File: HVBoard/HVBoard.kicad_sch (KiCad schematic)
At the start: 40 parts, among them J1 Conn_01x03_Pin, J2 Conn_01x08_Pin, K1 G2RL-1A-E-HA DC5, K2 G2RL-1A-E-HA DC5, Q1 NMOS, Q2 NMOS, Q3 BTA16-600B, Q4 NMOS, Q5 BTA16-600B, Q6 NMOS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

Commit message: More work
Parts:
- removed C1, C2: 0.01u, symbol Device:C_Polarized
- removed J1: Conn_01x03_Pin, symbol Connector:Conn_01x03_Pin
- removed PS1: TMLM04105, Converter_ACDC:Converter_ACDC_TRACO_TMLM-04_THT, symbol Converter_ACDC:TMLM04105
- added C1, C3: 0.01u, Capacitor_THT:C_Rect_L13.0mm_W4.0mm_P10.00mm_FKS3_FKP3_MKS4, symbol Device:C
- added H5, H6: MountingHole, MountingHole:MountingHole_3.2mm_M3, symbol Mechanical:MountingHole
- added J1: Conn_01x08_Pin, Connector_PinHeader_2.54mm:PinHeader_1x08_P2.54mm_Vertical, symbol Connector:Conn_01x08_Pin
- added J3: B3P-VH__LF__SN_, HWBoard:HDRV3W114P0X396_1X3_1182X850X1090P, symbol B3P-VH:B3P-VH__LF__SN_
- added J4, J5: Conn_01x02_Pin, symbol Connector:Conn_01x02_Pin
- added J6: Conn_01x03_Pin, symbol Connector:Conn_01x03_Pin
- added R16: R, Resistor_SMD:R_0603_1608Metric_Pad0.98x0.95mm_HandSolder, symbol Device:R
- added U4: 5V700mA 3.5W, wx-dc12003:WX-DC12003, symbol WX-DC12003:WX-DC12003
- Q1, Q2, Q4, Q6: footprint (none) -> Package_TO_SOT_SMD:SOT-23
- R11, R14, R3, R5, R6, R9: footprint (none) -> Resistor_SMD:R_1206_3216Metric_Pad1.30x1.75mm_HandSolder
- R13, R8: footprint (none) -> Resistor_THT:R_Axial_DIN0207_L6.3mm_D2.5mm_P10.16mm_Horizontal
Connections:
- net +3.3V: now also R16.2
- net +5V: now also J6.3 (Pin_3)
- net 120VAC_HOT: now also K1.13, U4.2 (L); no longer K1.14
- net 120VAC_HOT_SWITCHED: now also K1.14; no longer K1.13
- net 120VAC_NEUTRAL: now also K2.13, U4.1 (N); no longer K2.14
- net 120VAC_NEUTRAL_SWITCHED: now also K2.14, J3.3; no longer K2.13
- net ACDC_5V: now also U4.3 (V+)
- net BOILER_HOT_OUT: now also C1.2
- net GND: now also J1.8 (Pin_8), J5.1 (Pin_1), J6.1 (Pin_1), U4.4 (V-)
- net PUMP_HOT_OUT: now also C3.2, J3.1
- net at R13.2: now also C1.1
- net at R8.2: now also C3.1
- new net PRESSURE_SENSOR_SIG: J6.2 (Pin_2)
- new net STEAM_VALVE_IN: J5.2 (Pin_2), R16.1
- new net THERMISTOR_IN: J4.2 (Pin_2)
- new net THERMISTOR_OUT: J4.1 (Pin_1)
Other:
- note added: "Capacitors: MKT1822310405"
- note added: "Mounting holes"
- note added: "NTC Thermistor"
- note added: "Pump connector is B3P-VH"
- note added: "Resistors: 1W Metal Film"
- note added: "Steam Valve Switch"
- note removed: "Pump connector is B3P-VH?"

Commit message: More HV work
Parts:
- removed D2: D_Zener, symbol Device:D_Zener
- removed H1, H2, H3, H4: MountingHole_Pad_MP, symbol Mechanical:MountingHole_Pad_MP
- removed K2: G2RL-1A-E-HA DC5, Relay_THT:Relay_SPST_Omron_G2RL-1A-E, symbol Relay:G2RL-1A-E
- removed Q2: NMOS, Package_TO_SOT_SMD:SOT-23, symbol Simulation_SPICE:NMOS
- added D2: PTVS6V0S1UR-QX, Diode_SMD:Nexperia_CFP3_SOD-123W, symbol Diode:ESD5Zxx
- added D3: MP01EA06, Diode_SMD:D_SOD-123, symbol Device:D_Schottky
- added D4: LED, LED_SMD:LED_0603_1608Metric, symbol Device:LED
- added F1: 1A, symbol Device:Fuse
- added J7, J8: Screw_Terminal_01x02, TerminalBlock:TerminalBlock_bornier-2_P5.08mm, symbol Connector:Screw_Terminal_01x02
- added JP1: Jumper_2_Open, symbol Jumper:Jumper_2_Open
- added R17: 20k, Resistor_SMD:R_0603_1608Metric_Pad0.98x0.95mm_HandSolder, symbol Device:R
- added TP6: TestPoint, Connector_PinHeader_2.54mm:PinHeader_1x01_P2.54mm_Vertical, symbol Connector:TestPoint
- D1: footprint (none) -> Diode_SMD:D_SOD-123
- J1, J2: footprint Connector_PinHeader_2.54mm:PinHeader_1x08_P2.54mm_Vertical -> Connector_JST:JST_PH_B8B-PH-K_1x08_P2.00mm_Vertical
- J4, J5: footprint (none) -> Connector_JST:JST_XH_B2B-XH-AM_1x02_P2.50mm_Vertical
- J6: footprint (none) -> Connector_JST:JST_XH_B3B-XH-AM_1x03_P2.50mm_Vertical
- R12, R7: value 65 -> 220
- R2: value 10k -> 220; footprint Resistor_SMD:R_0603_1608Metric_Pad0.98x0.95mm_HandSolder -> Resistor_SMD:R_0603_1608Metric; Mouser # (none) -> 71-CRCW0603-665-E3; Mouser Link (none) -> https://www.mouser.com/ProductDetail/Vishay-Dale/CRCW060366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
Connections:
- net 120VAC_NEUTRAL_SWITCHED is gone; now on net 120VAC_NEUTRAL: J3.3, R5.2
- net +3.3V: no longer J2.2 (Pin_2), R12.1, R4.1, R7.1
- net +5V: now also R12.1, R2.1, R4.2, R7.1, D3.1 (K)
- net 120VAC_HOT: now also J7.2 (Pin_2)
- net 120VAC_NEUTRAL: now also J7.1 (Pin_1), J8.2 (Pin_2)
- net ACDC_5V: now also JP1.1 (A); no longer J2.3 (Pin_3)
- net AC_RELAYS: now also J2.2 (Pin_2); no longer J2.4 (Pin_4), R2.1
- net AC_ZC: now also J2.3 (Pin_3), R4.1, R17.1; no longer J2.5 (Pin_5), R4.2
- net BOILER_HOT_OUT: now also J8.1 (Pin_1)
- net BOILER_TRIAC: now also J2.5 (Pin_5); no longer J2.7 (Pin_7)
- net GND: now also D2.2 (A), D4.1 (K), R17.2
- net PRESSURE_SENSOR_SIG: now also J2.7 (Pin_7)
- net PUMP_TRIAC: now also J2.4 (Pin_4); no longer J2.6 (Pin_6)
- net STEAM_VALVE_IN: now also J2.6 (Pin_6)
- net THERMISTOR_IN: now also J1.1 (Pin_1)
- net THERMISTOR_OUT: now also J1.2 (Pin_2)
- net at R2.2: now also D4.2 (A)
- new net: F1.1, JP1.2 (B)
- new net: D2.1 (K), D3.2 (A), F1.2, TP6.1
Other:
- note added: "BZT52C5V1-E3-18"
- note added: "No buffering on thermistor Need raw resistance"
- note added: "OEM sensor connectors are B2B-XH?"
- note added: "Out ~3.3v"
- note added: "Power LED"
- note added: "Power Protection TVS + Reverse Polarity"
- note added: "Power and boiler are soldered So use terminal blocks TB0221600000G"
- note removed: "Boiler is soldered"
- note removed: "Power is soldered"
- note removed: "Switch both in case of reverse polarity (ex. reversed plug)"
- moved on the sheet: H5, H6, J3, R4

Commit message: More HV work
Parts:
- removed J1: Conn_01x08_Pin, Connector_JST:JST_PH_B8B-PH-K_1x08_P2.00mm_Vertical, symbol Connector:Conn_01x08_Pin
- removed R16: R, Resistor_SMD:R_0603_1608Metric_Pad0.98x0.95mm_HandSolder, symbol Device:R
- added J9: Conn_01x02_Pin, Connector_JST:JST_XH_B2B-XH-AM_1x02_P2.50mm_Vertical, symbol Connector:Conn_01x02_Pin
- added R18: 10k, Resistor_SMD:R_0603_1608Metric_Pad0.98x0.95mm_HandSolder, symbol Device:R
- added R19: 20k, Resistor_SMD:R_0603_1608Metric_Pad0.98x0.95mm_HandSolder, symbol Device:R
- F1: footprint (none) -> Fuse:Fuse_0603_1608Metric_Pad1.05x0.95mm_HandSolder
- JP1: footprint (none) -> Jumper:SolderJumper-2_P1.3mm_Open_Pad1.0x1.5mm
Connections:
- net +5V: now also R18.2
- net GND: now also R19.2
- net STEAM_VALVE_IN: now also R18.1, R19.1
- net THERMISTOR_IN: now also J9.1 (Pin_1)
- net THERMISTOR_OUT: now also J9.2 (Pin_2)

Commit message: More HV work
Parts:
- added R16, R20, R21: 10k, Resistor_SMD:R_0603_1608Metric_Pad0.98x0.95mm_HandSolder, symbol Device:R
- R1: value 10k -> 1k
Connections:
- net +5V: now also TP6.1
- net GND: now also R16.1, R20.1, R21.1
- net at D2.1 (K), D3.2 (A), F1.2: no longer TP6.1
- net at Q1.2 (G), R1.2: now also R16.2
- net at Q6.2 (G), R15.2: now also R21.2
- net at Q4.2 (G), R10.2: now also R20.2
- net ACDC_5V: no longer names the net of JP1.1 (A), U4.3 (V+)
- net THERMISTOR_IN: no longer names the net of J4.2 (Pin_2), J9.1 (Pin_1)
- net THERMISTOR_OUT: no longer names the net of J4.1 (Pin_1), J9.2 (Pin_2)
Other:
- note added: "+5V"
- note added: "Connector to controller"
- note added: "Connector to thermistor"
- note added: "LV Sensor Connection"
- moved on the sheet: C1, C3, D2, D3, D4, F1, H5, H6, J2, J4, J5, J6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

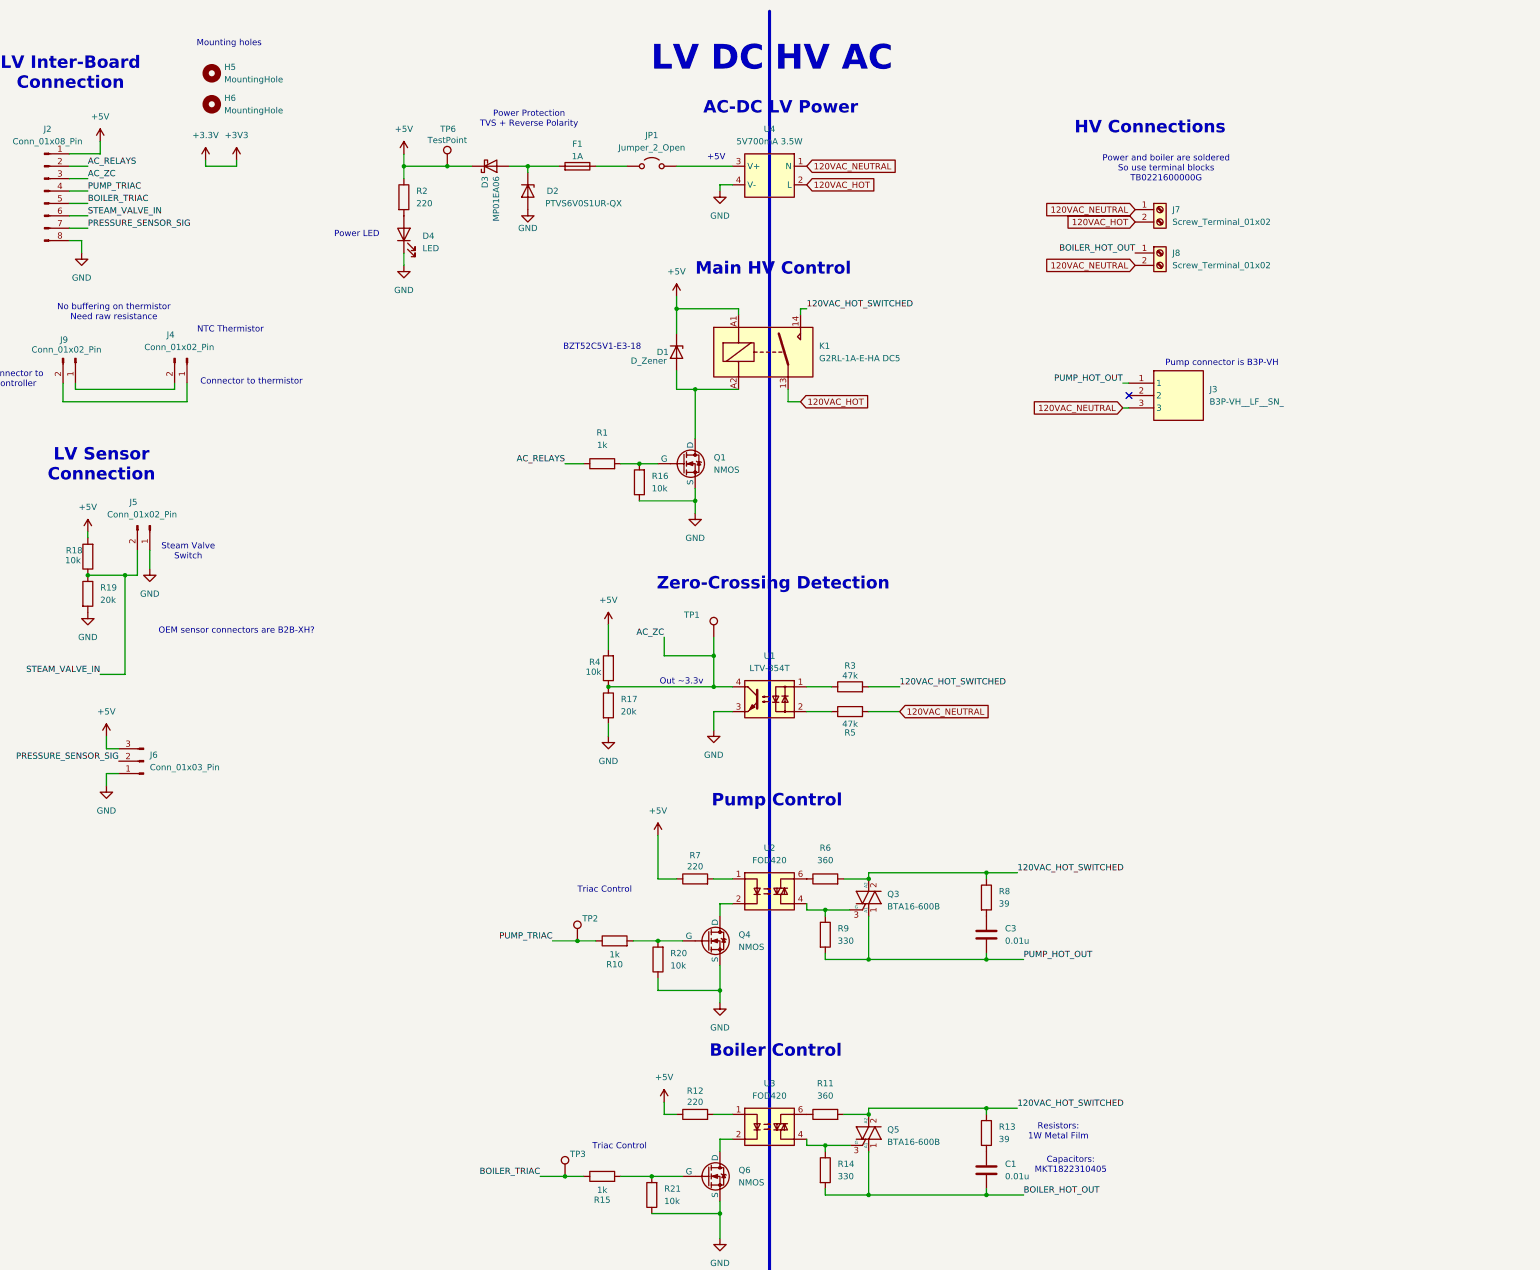
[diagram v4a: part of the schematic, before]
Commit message: Reddit feedback integrated into HV board
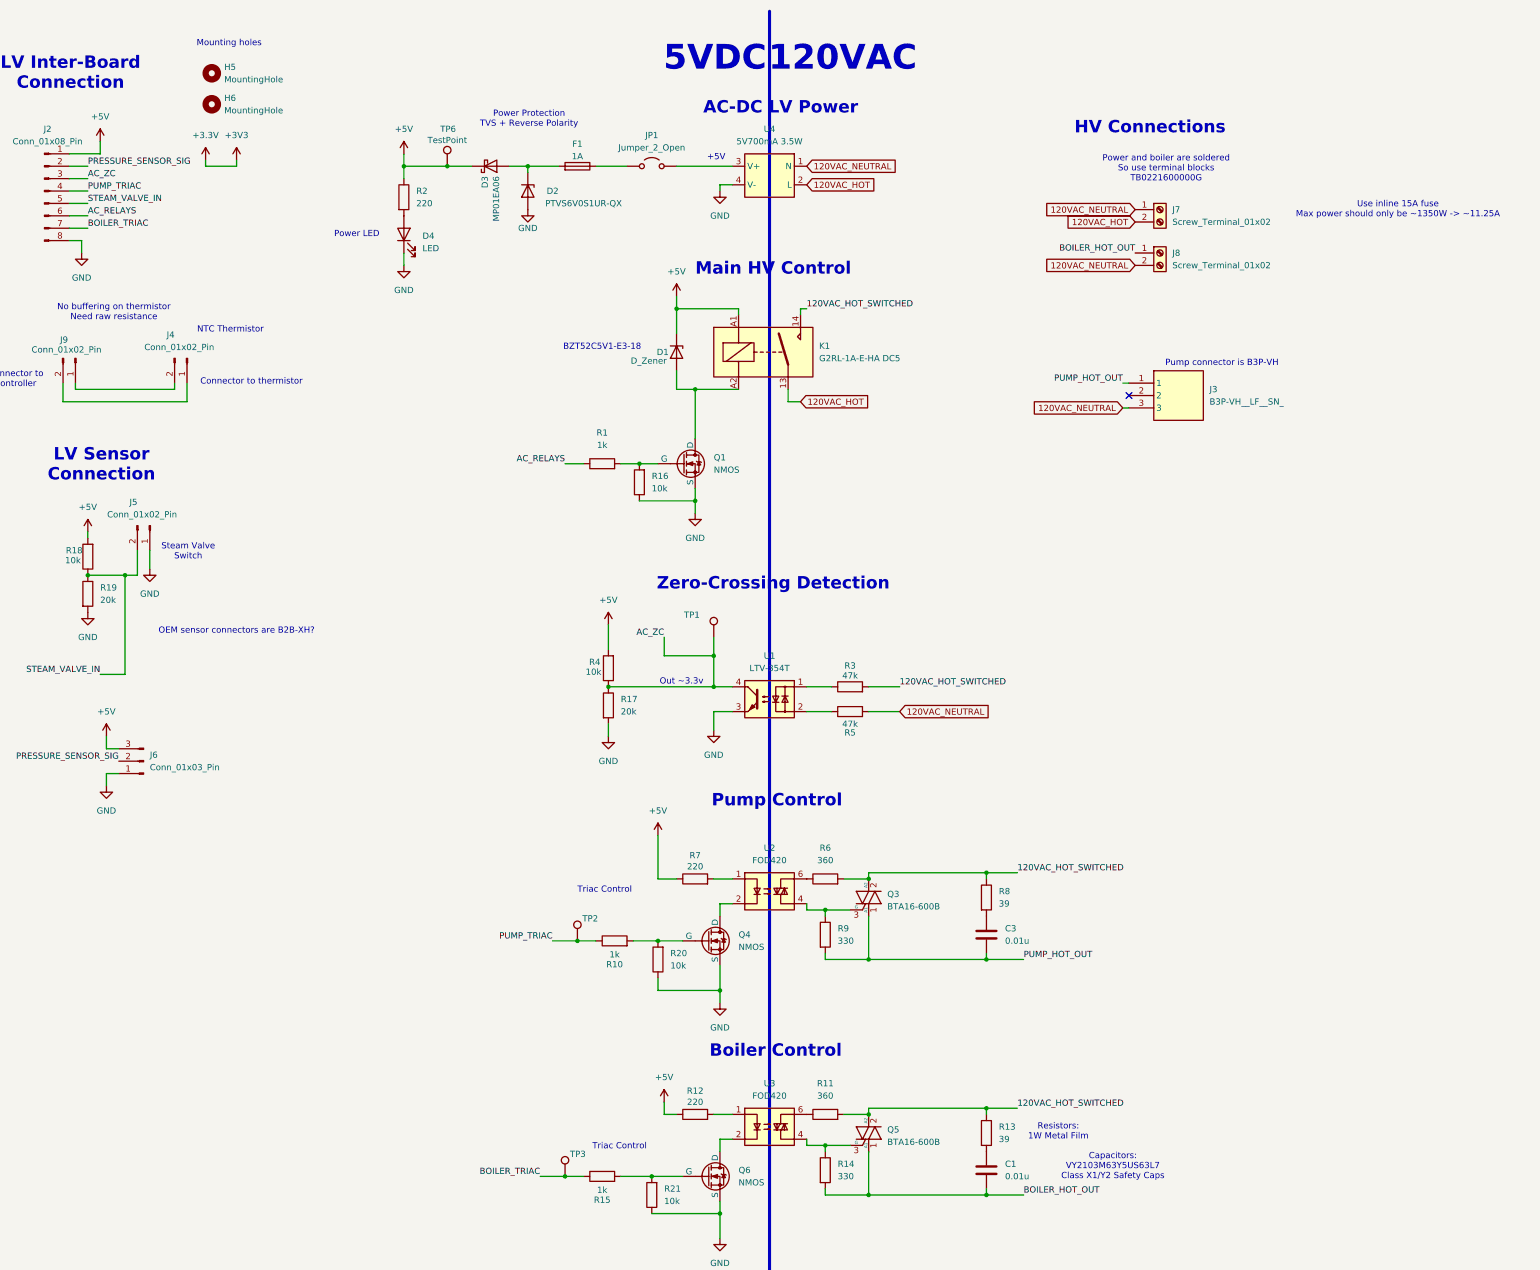
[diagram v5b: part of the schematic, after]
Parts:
- C1, C3: footprint Capacitor_THT:C_Rect_L13.0mm_W4.0mm_P10.00mm_FKS3_FKP3_MKS4 -> Capacitor_THT:C_Disc_D11.0mm_W5.0mm_P7.50mm
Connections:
- net AC_RELAYS: now also J2.6 (Pin_6); no longer J2.2 (Pin_2)
- net BOILER_TRIAC: now also J2.7 (Pin_7); no longer J2.5 (Pin_5)
- net PRESSURE_SENSOR_SIG: now also J2.2 (Pin_2); no longer J2.7 (Pin_7)
- net STEAM_VALVE_IN: now also J2.5 (Pin_5); no longer J2.6 (Pin_6)
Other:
- note added: "120VAC"
- note added: "5VDC"
- note added: "Capacitors: VY2103M63Y5US63L7 Class X1/Y2 Safety Caps"
- note added: "Use inline 15A fuse Max power should only be ~1350W -> ~11.25A"
- note removed: "Capacitors: MKT1822310405"
- note removed: "HV AC"
- note removed: "LV DC"
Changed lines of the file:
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@@
 		)
 	)
-	(text "LV DC"
+	(text "5VDC"
 		(exclude_from_sim no)
-		(at 163.83 19.812 0)
+		(at 165.354 19.812 0)
 		(effects
 			(font
@@
 		)
 	)
+	(text "Use inline 15A fuse\nMax power should only be ~1350W -> ~11.25A"
+		(exclude_from_sim no)
+		(at 305.308 50.8 0)
+		(effects
+			(font
+				(size 1.27 1.27)
+			)
+		)
+	)
 	(text "BZT52C5V1-E3-18\n"
 		(exclude_from_sim no)
@@
 		)
 	)
-	(text "Capacitors:\nMKT1822310405"
+	(text "Capacitors:\nVY2103M63Y5US63L7\nClass X1/Y2 Safety Caps"
 		(exclude_from_sim no)
-		(at 238.252 246.634 0)
+		(at 246.888 246.888 0)
 		(effects
 			(font
@@
 		)
 	)
-	(text "HV AC"
+	(text "120VAC"
 		(exclude_from_sim no)
-		(at 189.738 19.812 0)
+		(at 191.516 19.812 0)
 		(effects
 			(font
@@
 		)
 	)
-	(label "120VAC_HOT_SWITCHED"
-		(at 203.2 148.59 0)
+	(label "PRESSURE_SENSOR_SIG"
+		(at 36.83 41.91 0)
 		(fields_autoplaced yes)
 		(effects
@@
 		)
 	)
-	(label "STEAM_VALVE_IN"
-		(at 39.37 146.05 180)
+	(label "120VAC_HOT_SWITCHED"
+		(at 203.2 148.59 0)
 		(fields_autoplaced yes)
 		(effects
@@
 				(size 1.27 1.27)
 			)
-			(justify right bottom)
+			(justify left bottom)
 		)
 	)
-	(label "AC_RELAYS"
-		(at 134.62 102.87 180)
+	(label "STEAM_VALVE_IN"
+		(at 39.37 146.05 180)
 		(fields_autoplaced yes)
 		(effects
@@
 		)
 	)
-	(label "120VAC_HOT_SWITCHED"
-		(at 184.15 71.12 0)
+	(label "AC_RELAYS"
+		(at 134.62 102.87 180)
 		(fields_autoplaced yes)
 		(effects
@@
 				(size 1.27 1.27)
 			)
-			(justify left bottom)
+			(justify right bottom)
 		)
 	)
-	(label "STEAM_VALVE_IN"
+	(label "AC_RELAYS"
 		(at 36.83 52.07 0)
 		(fields_autoplaced yes)
@@
 	)
 	(label "120VAC_HOT_SWITCHED"
-		(at 227.33 234.95 0)
+		(at 184.15 71.12 0)
 		(fields_autoplaced yes)
 		(effects
@@
 		)
 	)
-	(label "PRESSURE_SENSOR_SIG"
-		(at 36.83 54.61 0)
+	(label "120VAC_HOT_SWITCHED"
+		(at 227.33 234.95 0)
 		(fields_autoplaced yes)
 		(effects
@@
 		)
 	)
-	(label "AC_RELAYS"
-		(at 36.83 41.91 0)
+	(label "PUMP_HOT_OUT"
+		(at 248.92 86.36 180)
 		(fields_autoplaced yes)
 		(effects
@@
 				(size 1.27 1.27)
 			)
-			(justify left bottom)
+			(justify right bottom)
 		)
 	)
-	(label "PUMP_HOT_OUT"
-		(at 248.92 86.36 180)
+	(label "BOILER_HOT_OUT"
+		(at 228.6 252.73 0)
 		(fields_autoplaced yes)
 		(effects
@@
 				(size 1.27 1.27)
 			)
-			(justify right bottom)
+			(justify left bottom)
 		)
 	)
 	(label "BOILER_TRIAC"
-		(at 36.83 49.53 0)
+		(at 36.83 54.61 0)
 		(fields_autoplaced yes)
 		(effects
@@
 		)
 	)
-	(label "BOILER_HOT_OUT"
-		(at 228.6 252.73 0)
+	(label "STEAM_VALVE_IN"
+		(at 36.83 49.53 0)
 		(fields_autoplaced yes)
 		(effects
@@
 			)
 		)
-		(property "Footprint" "Capacitor_THT:C_Rect_L13.0mm_W4.0mm_P10.00mm_FKS3_FKP3_MKS4"
+		(property "Footprint" "Capacitor_THT:C_Disc_D11.0mm_W5.0mm_P7.50mm"
 			(at 221.9452 251.46 0)
 			(effects
@@
 			)
 		)
-		(property "Footprint" "Capacitor_THT:C_Rect_L13.0mm_W4.0mm_P10.00mm_FKS3_FKP3_MKS4"
+		(property "Footprint" "Capacitor_THT:C_Disc_D11.0mm_W5.0mm_P7.50mm"
 			(at 221.9452 203.2 0)
 			(effects

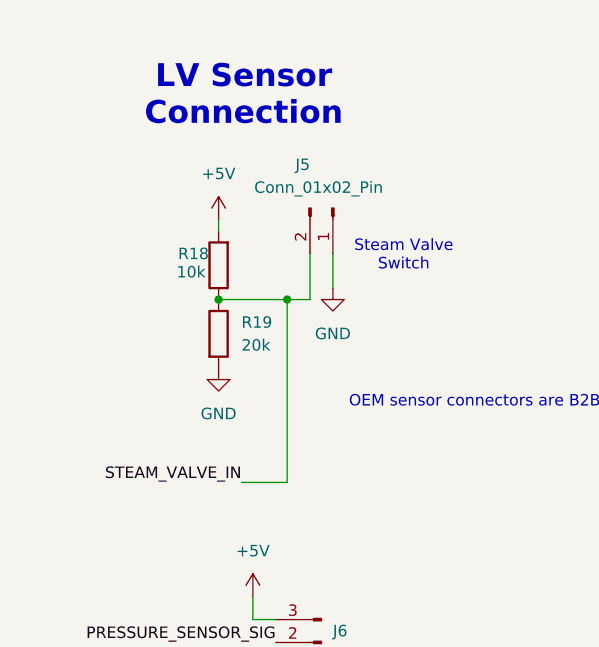
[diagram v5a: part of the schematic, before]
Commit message: Boards finalized and ordered
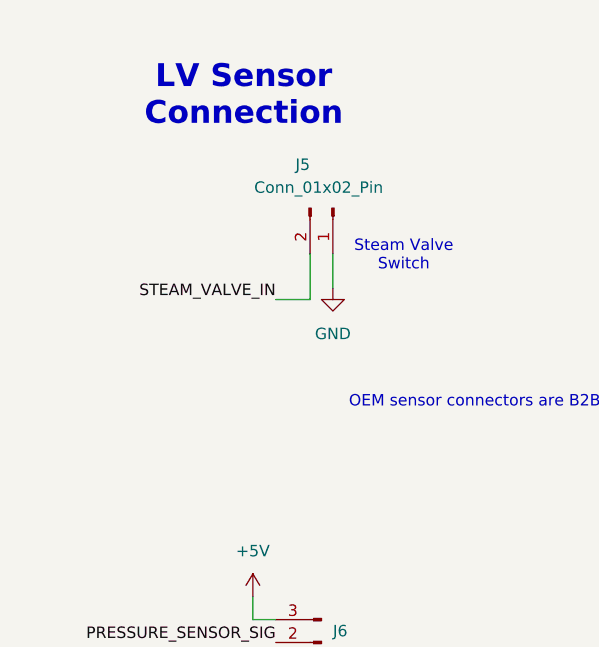
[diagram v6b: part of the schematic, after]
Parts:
- removed R18: 10k, Resistor_SMD:R_0603_1608Metric_Pad0.98x0.95mm_HandSolder, symbol Device:R
- removed R19: 20k, Resistor_SMD:R_0603_1608Metric_Pad0.98x0.95mm_HandSolder, symbol Device:R
